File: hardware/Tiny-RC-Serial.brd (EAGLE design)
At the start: 27.9 x 27.9 mm, 16 parts, among them IC1 ATTINY84A-SSU, Y1 20Mhz

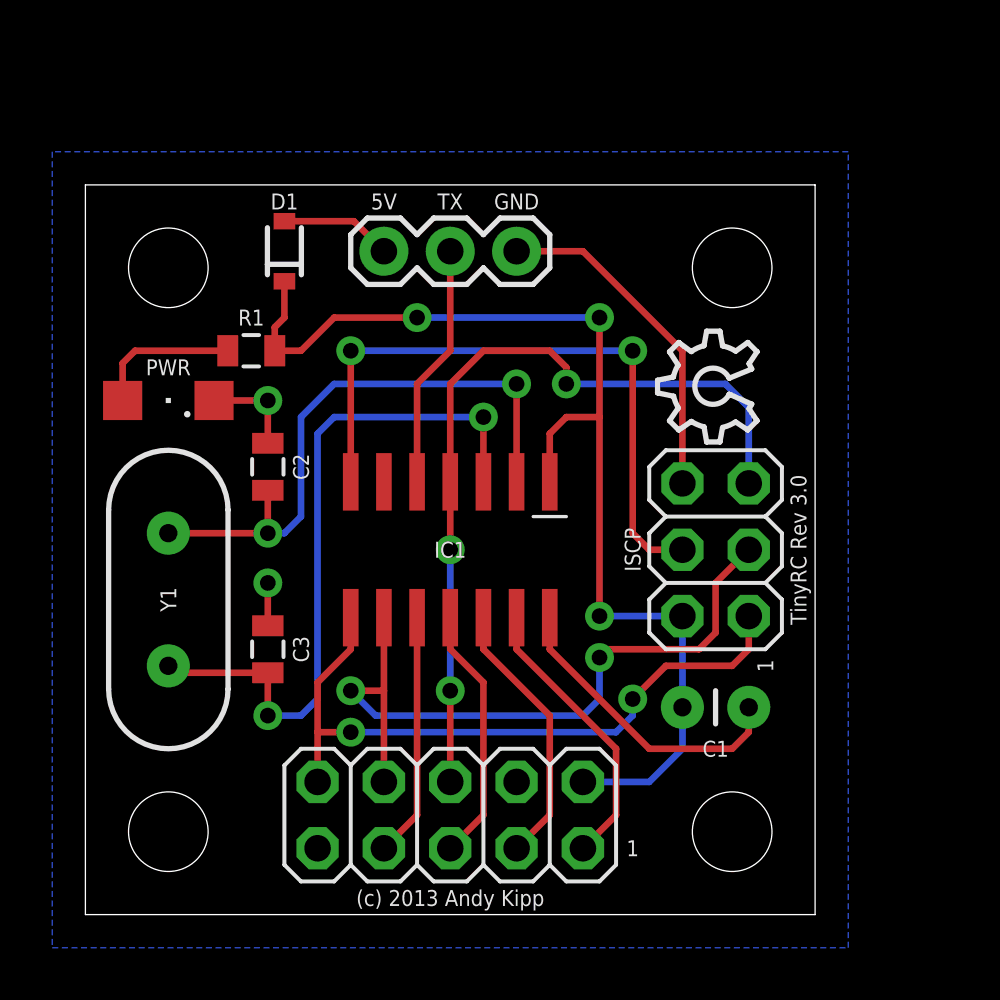
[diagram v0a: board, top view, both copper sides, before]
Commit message: updated board to rev 3.0 - now using ATTiny2313
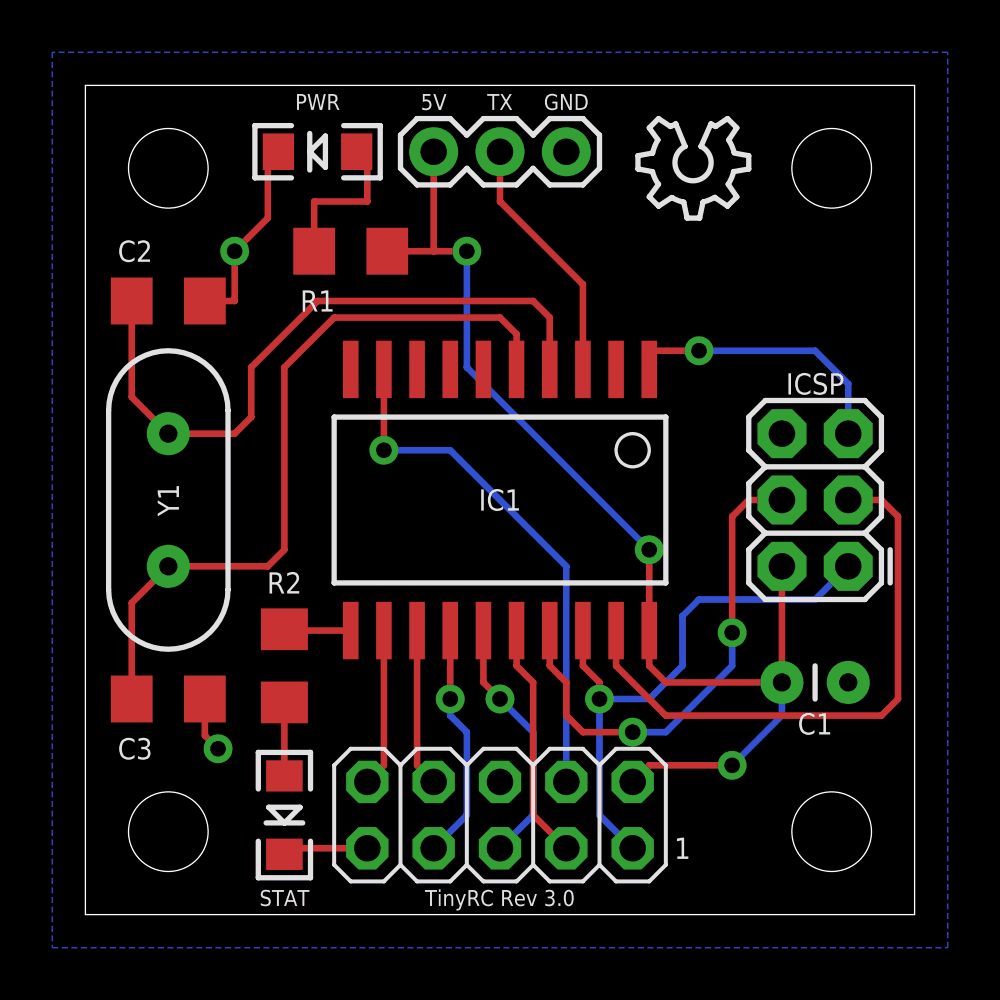
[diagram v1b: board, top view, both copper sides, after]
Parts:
- removed D1: (no value), SparkFun:SOD-323
- removed IC1: ATTINY84A-SSU, attiny:SO14
- removed JP2: (no value), pinhead:2X03
- removed LED1: (no value), led:SML1206
- added J1: ICSP, SparkFun-Connectors:2X3
- added PWR, STAT: (no value), SparkFun-LED:LED-1206
- added R2: 330, SparkFun-Resistors:1206
- added U1: ATTINY2313A, SparkFun-DigitalIC:SOP20W
- C2, C3: device SparkFun-Capacitors:0805 -> SparkFun-Capacitors:1206
- R1: device SparkFun-Resistors:0805 -> SparkFun-Resistors:1206
- moved U$5 12.4 mm to (25.4, 30.5), turned to 180 degrees
- moved C2 7.41 mm to (3.17, 23.5), turned to 0 degrees
- moved R1 5.39 mm to (10.2, 25.4)
- moved S2 5.39 mm to (28.6, 28.6)
- moved JP3 4.26 mm to (18.4, 29.2)
- moved C3 4.26 mm to (3.17, 8.26), turned to 0 degrees
- moved C1 3.93 mm to (26.7, 8.89)
- moved Y1 3.81 mm to (3.17, 15.9)
- moved S3 3.81 mm to (28.6, 3.17)
- moved S4 3.81 mm to (3.17, 28.6)
- moved JP1 1.90 mm to (15.9, 3.81)
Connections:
- removed net VIN: D1.2, JP3.3
- new net MOSI: J1.4, U1.17
- new net N$5: R2.1, STAT.A
- new net RESET: J1.5, U1.1
- new net RX: U1.2
- new net SCK: J1.3, U1.19
- net 5V: now also J1.2, JP3.3, U1.20; no longer D1.1, IC1.1, JP2.2
- net GND: now also J1.6, PWR.C, STAT.C; no longer IC1.14, JP2.6, LED1.C
- net N$1: now also R2.2, U1.11; no longer IC1.7, JP2.4
- net N$2: now also PWR.A; no longer LED1.A
- net N$3: now also U1.4; no longer IC1.2
- net N$4: now also U1.5; no longer IC1.3
- net RC1: now also J1.1, U1.18; no longer IC1.13
- net RC2: now also U1.16; no longer IC1.12
- net RC3: now also U1.15; no longer IC1.11
- net RC4: now also U1.14; no longer IC1.10
- net RC5: now also U1.13; no longer IC1.9, JP2.3
- net RC6: now also U1.12; no longer IC1.8, JP2.1
- net RCDATA: now also JP1.3, U1.9; no longer IC1.4, JP1.5, JP2.5
- net TX: now also U1.3; no longer IC1.5
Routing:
- net SCK: track 0.00 -> 22.4 mm
- net N$1: track 24.4 -> 2.56 mm, vias 2 -> 0
- net RC5: track 27.9 -> 6.06 mm, vias 2 -> 0
- net RC6: track 26.3 -> 6.61 mm, vias 2 -> 0
- net MOSI: track 0.00 -> 19.1 mm, vias 0 -> 2
- net GND: track 30.0 -> 12.9 mm
- net RCDATA: track 31.4 -> 20.2 mm, vias 3 -> 1
- net RC1: track 10.9 -> 21.9 mm, vias 0 -> 1
- net RESET: track 0.00 -> 10.8 mm, vias 0 -> 1
- net VIN: track 4.29 -> 0.00 mm
- net N$5: track 0.00 -> 2.82 mm
- net N$3: track 23.3 -> 25.7 mm, vias 2 -> 0
- net N$4: track 27.0 -> 28.6 mm, vias 2 -> 0
- net RC2: track 10.4 -> 9.12 mm
- net RC4: track 9.36 -> 9.12 mm, vias 0 -> 1
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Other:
- board size 27.9 x 27.9 mm -> 31.8 x 31.8 mm
- board text added: "IC1"
- board text removed: "ISCP"
- board text removed: "PWR"

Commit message: Update hardware to 3.1
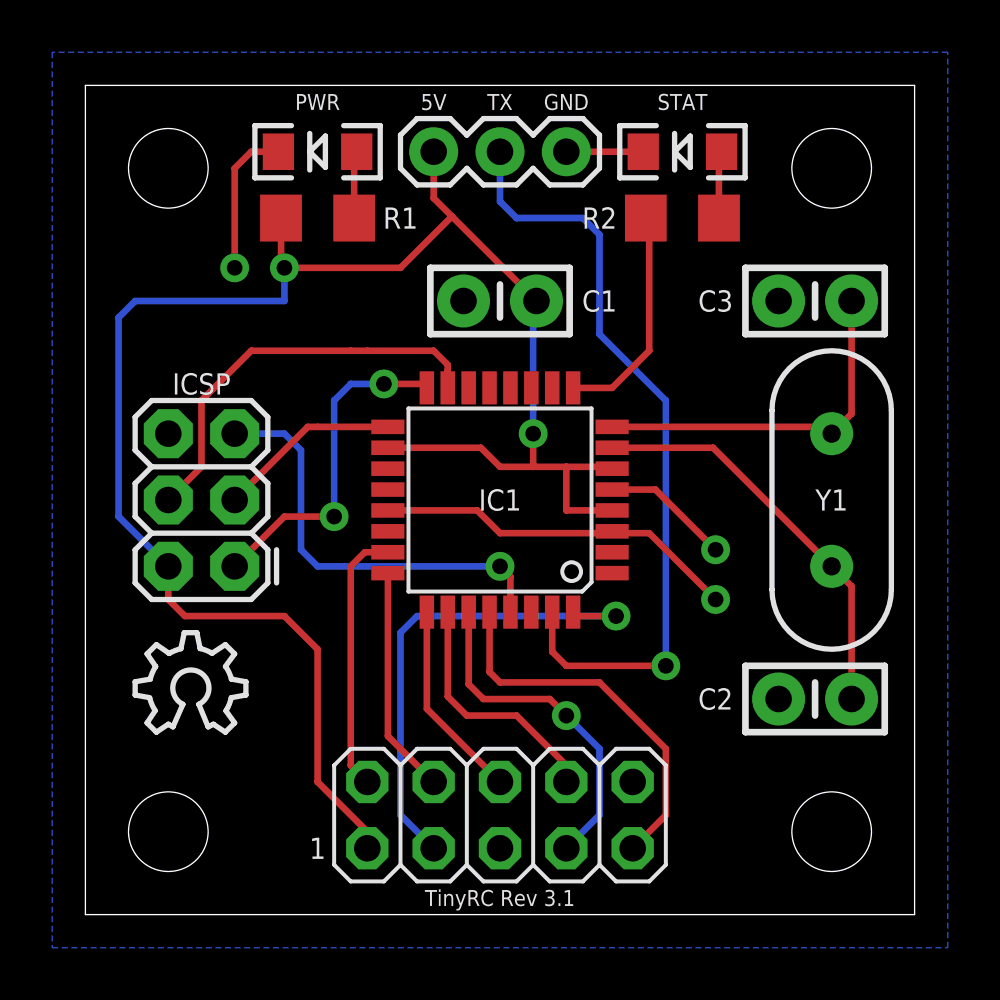
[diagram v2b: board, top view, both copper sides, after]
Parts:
- removed U1: ATTINY2313A, SparkFun-DigitalIC:SOP20W
- added IC1: ATMEGA328P, SparkFun-DigitalIC:TQFP32-08
- C1: device SparkFun:CAP-PTH-SMALL -> SparkFun-Capacitors:CAP-PTH-SMALL-KIT
- C2, C3: device SparkFun-Capacitors:1206 -> SparkFun-Capacitors:CAP-PTH-SMALL-KIT
- moved U$5 33.2 mm to (1.91, 6.99), turned to 0 degrees
- moved STAT 29.6 mm to (22.9, 29.2), turned to 180 degrees
- moved C2 29.1 mm to (27.9, 8.26), turned to 180 degrees
- moved C3 29.1 mm to (27.9, 23.5), turned to 180 degrees
- moved Y1 25.4 mm to (28.6, 15.9), turned to 270 degrees
- moved J1 23.5 mm to (5.71, 13.3)
- moved R2 22.9 mm to (22.9, 26.7), turned to 180 degrees
- moved C1 18.2 mm to (15.9, 23.5), turned to 180 degrees
- moved R1 1.80 mm to (8.89, 26.7), turned to 180 degrees
- turned JP1 to 0 degrees
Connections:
- new net MISO: IC1.16, J1.1
- net 5V: now also IC1.18, IC1.4, IC1.6; no longer U1.20
- net GND: now also IC1.21, IC1.3, IC1.5
- net MOSI: now also IC1.15; no longer U1.17
- net N$1: now also IC1.9; no longer U1.11
- net N$3: now also IC1.7; no longer U1.4
- net N$4: now also IC1.8; no longer U1.5
- net RC1: now also IC1.23; no longer J1.1, U1.18
- net RC2: now also IC1.24; no longer U1.16
- net RC3: now also IC1.25; no longer U1.15
- net RC4: now also IC1.26; no longer U1.14
- net RC5: now also IC1.27; no longer U1.13
- net RC6: now also IC1.28; no longer U1.12
- net RCDATA: now also IC1.32; no longer U1.9
- net RESET: now also IC1.29; no longer U1.1
- net RX: now also IC1.30; no longer U1.2
- net SCK: now also IC1.17; no longer U1.19
- net TX: now also IC1.31; no longer U1.3
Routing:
- net 5V: track 44.1 -> 69.8 mm, vias 3 -> 2
- net TX: track 9.65 -> 29.9 mm, vias 0 -> 1
- net SCK: track 22.4 -> 7.03 mm
- net N$4: track 28.6 -> 13.9 mm
- net GND: track 12.9 -> 27.6 mm, vias 2 -> 3
- net MISO: track 0.00 -> 12.9 mm, vias 0 -> 2
- net RC1: track 21.9 -> 10.2 mm, vias 1 -> 0
- net N$3: track 25.7 -> 15.7 mm
- net RC6: track 6.61 -> 14.6 mm
- net RC5: track 6.06 -> 13.1 mm, vias 0 -> 1
- net N$1: track 2.56 -> 8.64 mm
- net RESET: track 10.8 -> 16.4 mm
- net N$2: track 6.01 -> 2.58 mm
- net MOSI: track 19.1 -> 16.4 mm, vias 2 -> 0
- net RC3: track 9.65 -> 7.66 mm, vias 1 -> 0
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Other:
- board text added: "TinyRC Rev 3.1"
- board text removed: "IC1"
- board text removed: "TinyRC Rev 3.0"
